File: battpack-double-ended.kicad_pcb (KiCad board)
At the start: 2 copper layers, 38 x 18 mm, 15 parts

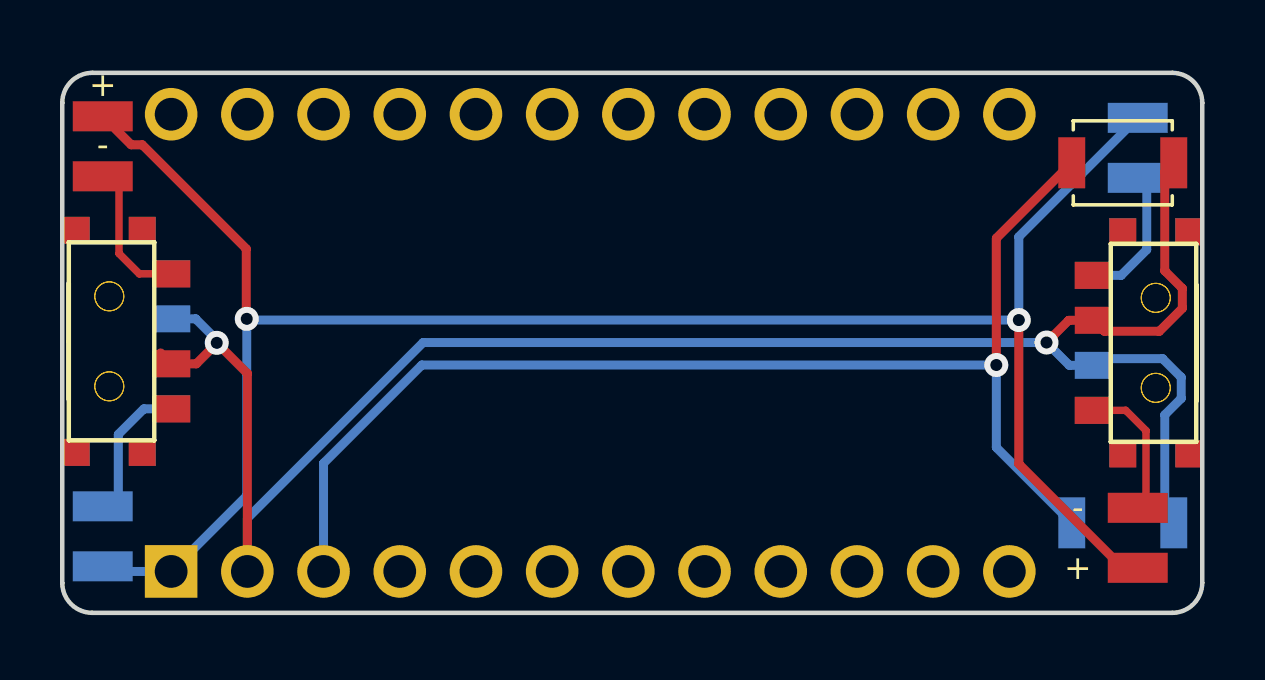
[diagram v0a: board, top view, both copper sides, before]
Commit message: Reduced size of PCB at original end in order to not overhand OLED pin locations on existing boards
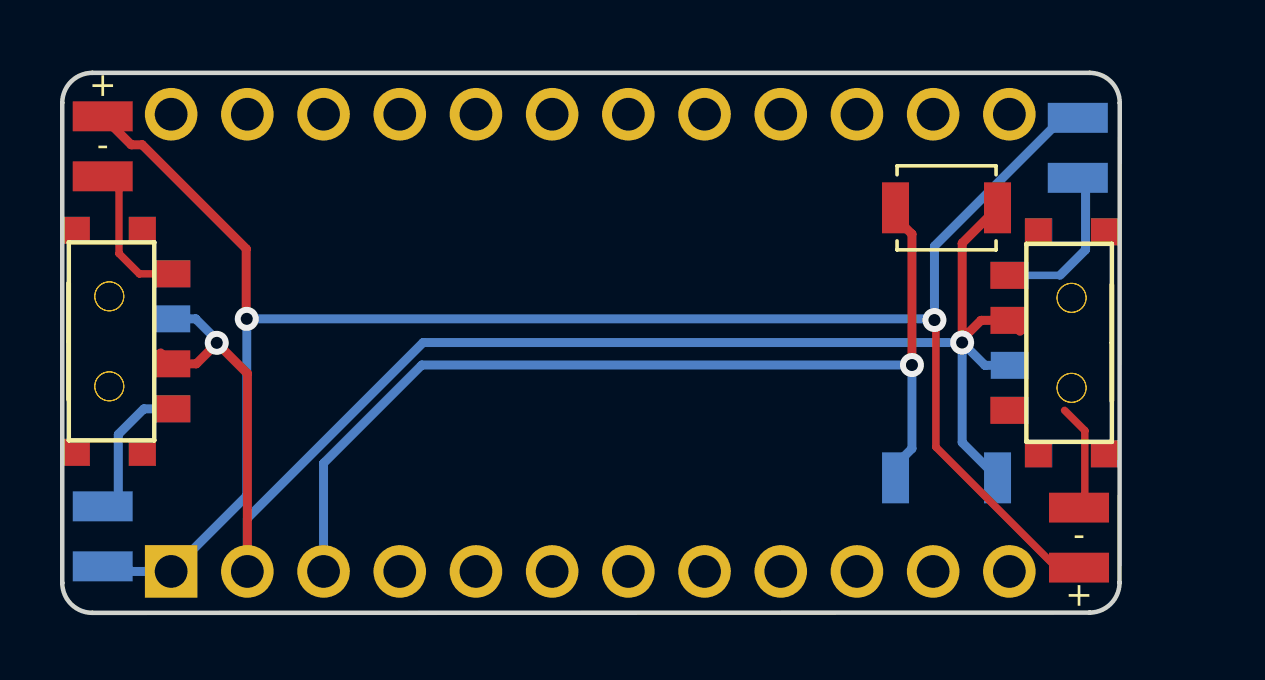
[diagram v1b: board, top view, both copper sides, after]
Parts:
- moved B1 6.06 mm to (75.7, 45.6)
- moved B2 6.06 mm to (75.7, 54.6)
- moved T2 2.81 mm to (79.9, 50.1)
- moved T1 2.80 mm to (79.9, 50.1)
- moved PAD1 2.00 mm to (80.1, 42.6)
- moved PAD2 2.00 mm to (80.1, 44.6)
- moved PAD3 1.96 mm to (80.1, 57.6)
- moved PAD4 1.96 mm to (80.1, 55.6)
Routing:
- net GND: track 64.3 -> 55.3 mm
- net RST: track 41.5 -> 34.5 mm
- net RAW: track 65.1 -> 63.5 mm
- net BAT: track 18.7 -> 18.0 mm
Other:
- board size 38 x 18 mm -> 35.2 x 18 mm
